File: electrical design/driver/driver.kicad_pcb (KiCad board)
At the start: 2 copper layers, 38 x 45 mm, 18 parts, among them J1 XT30PW-F, J2 PH2.0 6P, J3 SH1.0 8P, Q1 IRFR5410PbF, U1 VNH5050A-E

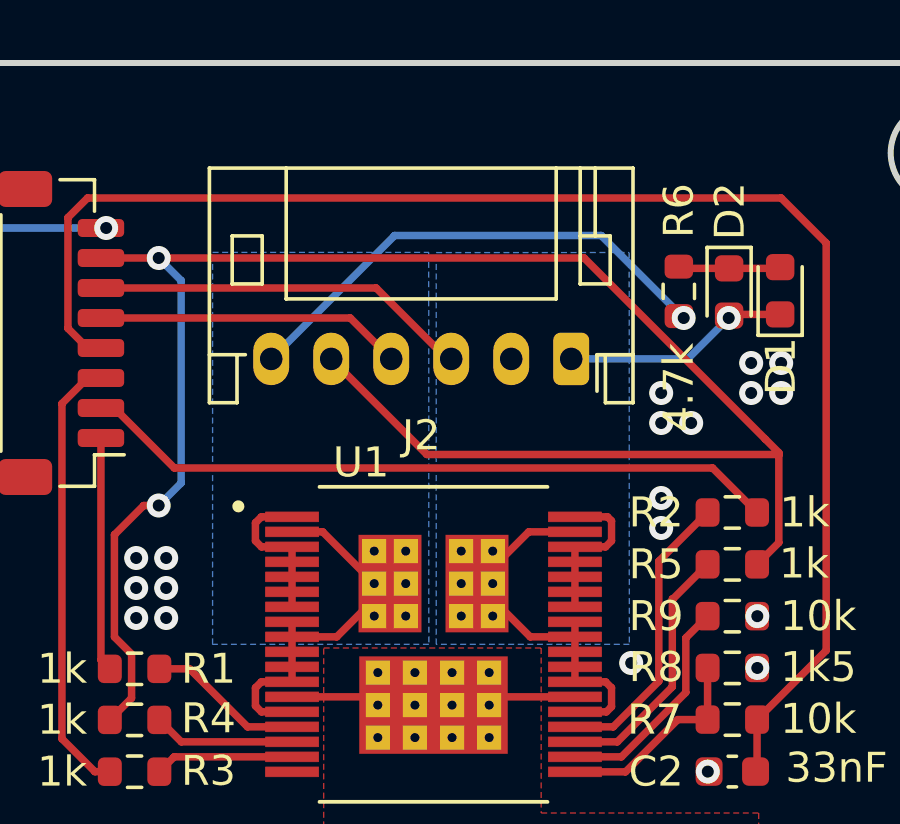
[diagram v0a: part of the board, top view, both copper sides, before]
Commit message: increase size of driver output polygon
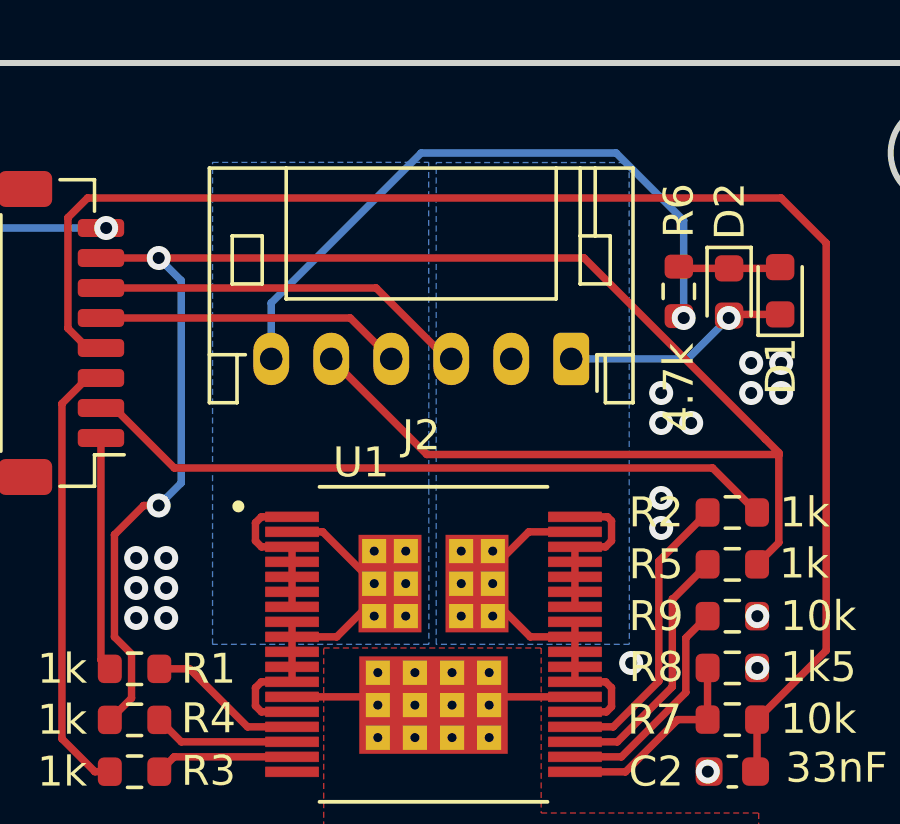
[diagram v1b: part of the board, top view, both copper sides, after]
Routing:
- net /OUTA: track 29.8 -> 35.1 mm
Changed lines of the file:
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@@
   (title_block
     (title "VNH5050A breakout board pcb drawing")
-    (date "2023-01-28")
-    (rev "1.0")
+    (date "2023-01-29")
+    (rev "1.1")
     (company "8076 Robotics")
   )
@@
   (segment (start 105.695 104.62815) (end 105.695 106.62815) (width 0.25) (layer "F.Cu") (net 10))
   (via (at 118.75 94.5) (size 0.8) (drill 0.4) (layers "F.Cu" "B.Cu") (net 10))
-  (segment (start 116 91.75) (end 118.75 94.5) (width 0.25) (layer "B.Cu") (net 10))
-  (segment (start 109.11375 91.75) (end 116 91.75) (width 0.25) (layer "B.Cu") (net 10))
-  (segment (start 105 95.86375) (end 109.11375 91.75) (width 0.25) (layer "B.Cu") (net 10))
+  (segment (start 116.5 89) (end 118.75 91.25) (width 0.25) (layer "B.Cu") (net 10))
+  (segment (start 105 95.86375) (end 105 94) (width 0.25) (layer "B.Cu") (net 10))
+  (segment (start 105 94) (end 110 89) (width 0.25) (layer "B.Cu") (net 10))
+  (segment (start 118.75 91.25) (end 118.75 94.5) (width 0.25) (layer "B.Cu") (net 10))
+  (segment (start 110 89) (end 116.5 89) (width 0.25) (layer "B.Cu") (net 10))
   (segment (start 99.325 105.89845) (end 99.6207 106.19415) (width 0.25) (layer "F.Cu") (net 11))
   (segment (start 99.325 98.5) (end 99.325 105.89845) (width 0.25) (layer "F.Cu") (net 11))
@@
         (xy 110.257065 105.377234)
         (xy 103.0457 105.37815)
-        (xy 103.045986 92.312814)
-        (xy 110.249342 92.311898)
+        (xy 103.045606 89.312814)
+        (xy 110.248962 89.311898)
       )
     )
@@
         (xy 116.93832 105.376907)
         (xy 110.4989 105.378089)
-        (xy 110.498839 92.318317)
-        (xy 116.93025 92.317135)
+        (xy 110.498288 89.318317)
+        (xy 116.929699 89.317135)
       )
     )

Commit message: submit all pcbs for production
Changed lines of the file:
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@@
       (layerselection 0x00010fc_ffffffff)
       (disableapertmacros false)
-      (usegerberextensions false)
+      (usegerberextensions true)
       (usegerberattributes true)
-      (usegerberadvancedattributes true)
-      (creategerberjobfile true)
+      (usegerberadvancedattributes false)
+      (creategerberjobfile false)
       (svguseinch false)
       (svgprecision 6)
@@
       (plotinvisibletext false)
       (sketchpadsonfab false)
-      (subtractmaskfromsilk false)
+      (subtractmaskfromsilk true)
       (outputformat 1)
       (mirror false)
-      (drillshape 1)
+      (drillshape 0)
       (scaleselection 1)
-      (outputdirectory "")
+      (outputdirectory "fab/")
     )
   )
@@
     (pad "8" smd roundrect (at 3.5 1.325 90) (size 0.6 1.55) (layers "F.Cu" "F.Paste" "F.Mask") (roundrect_rratio 0.25)
       (net 2 "GND") (pinfunction "Pin_8") (pintype "passive"))
-    (pad "MP" smd roundrect (at 4.8 -1.2 90) (size 1.2 1.8) (layers "F.Cu" "F.Paste" "F.Mask") (roundrect_rratio 0.208333))
-    (pad "MP" smd roundrect (at -4.8 -1.2 90) (size 1.2 1.8) (layers "F.Cu" "F.Paste" "F.Mask") (roundrect_rratio 0.208333))
+    (pad "MP" smd roundrect (at 4.8 -1.2 90) (size 1.2 1.8) (layers "F.Cu" "F.Paste" "F.Mask") (roundrect_rratio 0.2083333333))
+    (pad "MP" smd roundrect (at -4.8 -1.2 90) (size 1.2 1.8) (layers "F.Cu" "F.Paste" "F.Mask") (roundrect_rratio 0.2083333333))
     (model "${KICAD6_3DMODEL_DIR}/Connector_JST.3dshapes/JST_SH_BM08B-SRSS-TB_1x08-1MP_P1.00mm_Vertical.wrl"
       (offset (xyz 0 0 0))
@@
   (segment (start 121.9207 98.988212) (end 121.9207 99.0793) (width 0.25) (layer "F.Cu") (net 9))
   (segment (start 101.25 92.5) (end 115.432488 92.5) (width 0.25) (layer "F.Cu") (net 9))
-  (segment (start 121.466244 98.533756) (end 121.9207 98.988212) (width 0.25) (layer "F.Cu") (net 9))
+  (segment (start 115.432488 92.5) (end 121.9207 98.988212) (width 0.25) (layer "F.Cu") (net 9))
   (segment (start 99.775 101.725) (end 100.75 100.75) (width 0.25) (layer "F.Cu") (net 9))
   (segment (start 121.9207 101.98735) (end 121.1957 102.71235) (width 0.25) (layer "F.Cu") (net 9))
@@
   (segment (start 99.325 92.5) (end 101.25 92.5) (width 0.25) (layer "F.Cu") (net 9))
   (segment (start 100.75 100.75) (end 101.25 100.75) (width 0.25) (layer "F.Cu") (net 9))
-  (segment (start 115.432488 92.5) (end 121.466244 98.533756) (width 0.25) (layer "F.Cu") (net 9))
   (segment (start 99.775 105.130988) (end 99.775 101.725) (width 0.25) (layer "F.Cu") (net 9))
   (segment (start 99.6207 107.89595) (end 100.3457 107.17095) (width 0.25) (layer "F.Cu") (net 9))
   (segment (start 107 95.86375) (end 110.18625 99.05) (width 0.25) (layer "F.Cu") (net 9))
   (segment (start 100.3457 105.701688) (end 99.775 105.130988) (width 0.25) (layer "F.Cu") (net 9))
-  (segment (start 99.6207 107.89595) (end 99.60405 107.89595) (width 0.25) (layer "F.Cu") (net 9))
-  (segment (start 99.60405 107.89595) (end 99.5 108) (width 0.25) (layer "F.Cu") (net 9))
   (segment (start 100.3457 107.17095) (end 100.3457 105.701688) (width 0.25) (layer "F.Cu") (net 9))
   (via (at 101.25 100.75) (size 0.8) (drill 0.4) (layers "F.Cu" "B.Cu") (net 9))

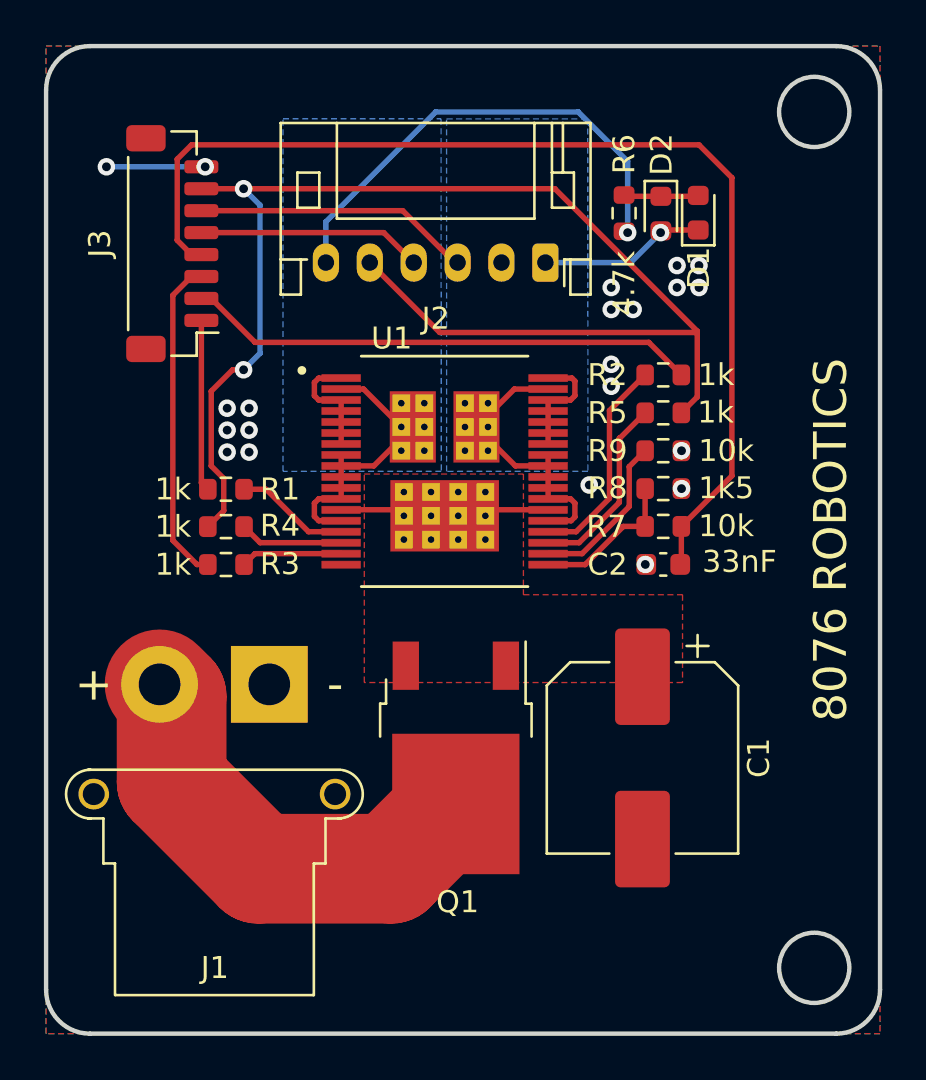
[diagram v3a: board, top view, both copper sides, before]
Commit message: fillet pcb traces
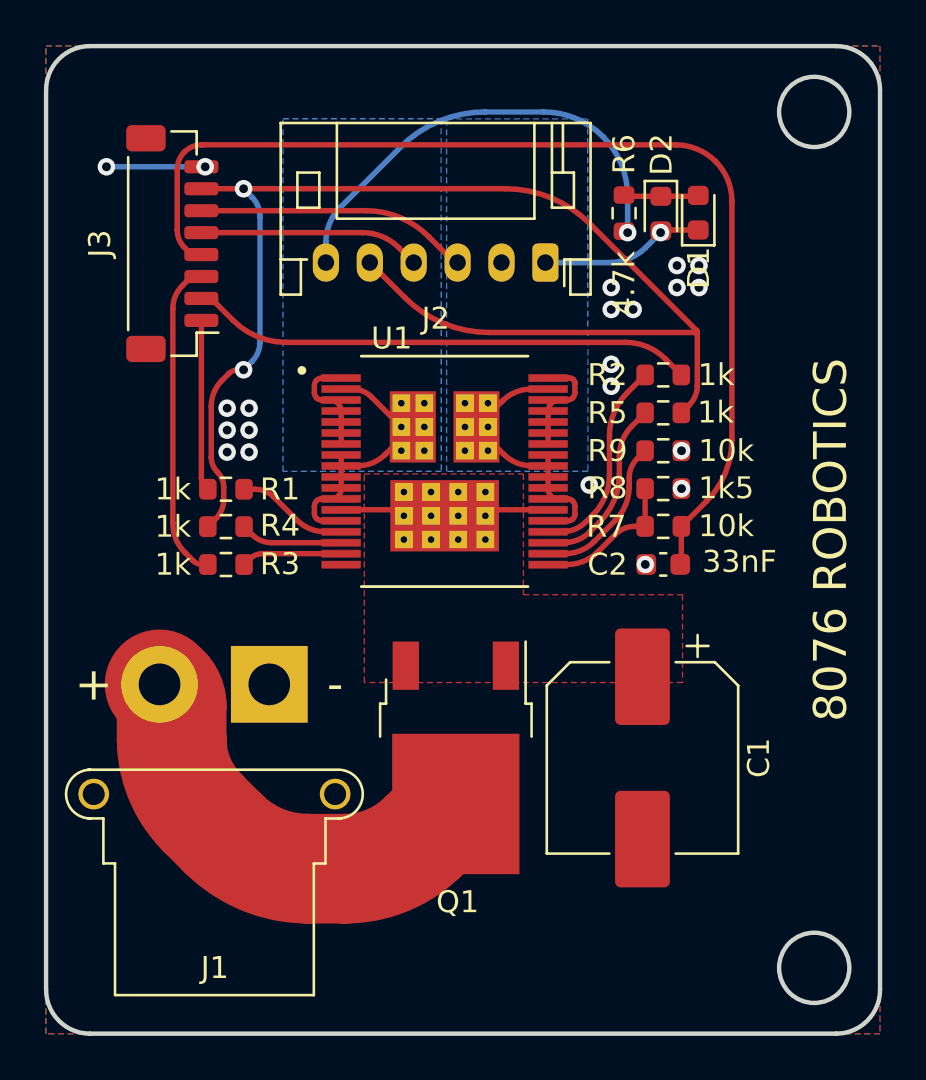
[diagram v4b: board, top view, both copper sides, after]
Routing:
- net /OUTA: track 35.1 -> 33.6 mm
- net +3V3: track 63.0 -> 62.0 mm
- net +12V: track 20.5 -> 19.7 mm
- net /CS: track 49.8 -> 49.2 mm
- net GND: track 15.0 -> 14.4 mm
- net /OUTB: track 20.7 -> 20.2 mm
